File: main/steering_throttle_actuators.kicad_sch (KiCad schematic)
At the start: 2 parts, among them M2 Throttle_Motor, M3 Steering_Motor

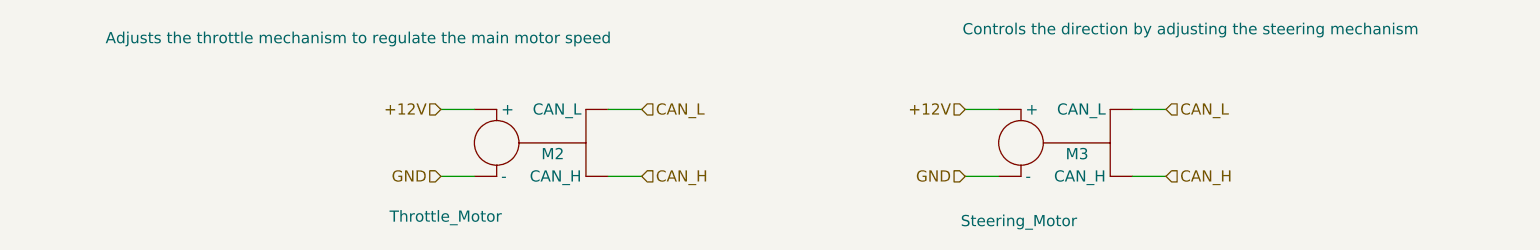
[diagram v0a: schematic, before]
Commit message: added cerbo gx and user interface sheet
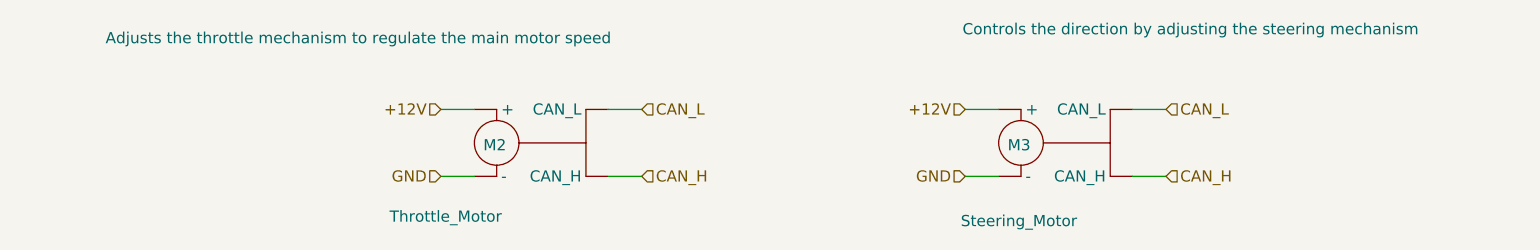
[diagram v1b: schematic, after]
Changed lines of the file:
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@@
 	)
 	(symbol
+		(lib_name "New_Library_0:Motor")
 		(lib_id "New_Library_0:Motor")
 		(at 157.48 90.17 0)
@@
 		(dnp no)
 		(property "Reference" "M3"
-			(at 162.56 91.4399 0)
+			(at 155.956 90.424 0)
 			(effects
 				(font
@@
 		(dnp no)
 		(property "Reference" "M2"
-			(at 102.87 91.4399 0)
+			(at 96.266 90.424 0)
 			(effects
 				(font

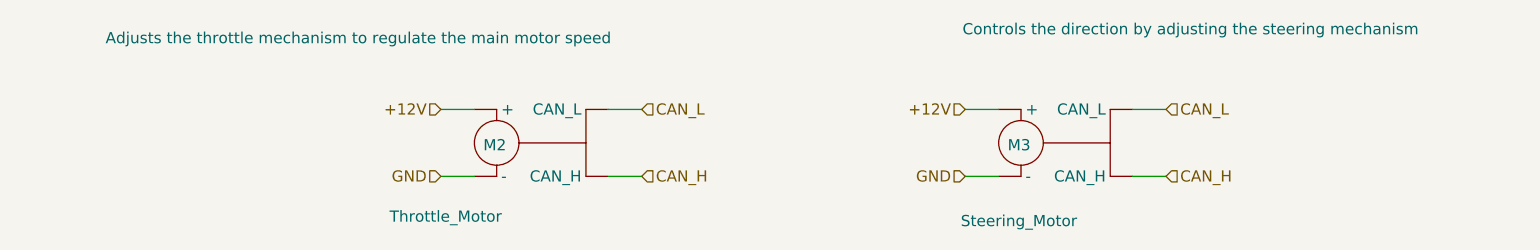
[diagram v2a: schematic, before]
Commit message: Changed name of Steering_Motor to Steering_Rod_Motor
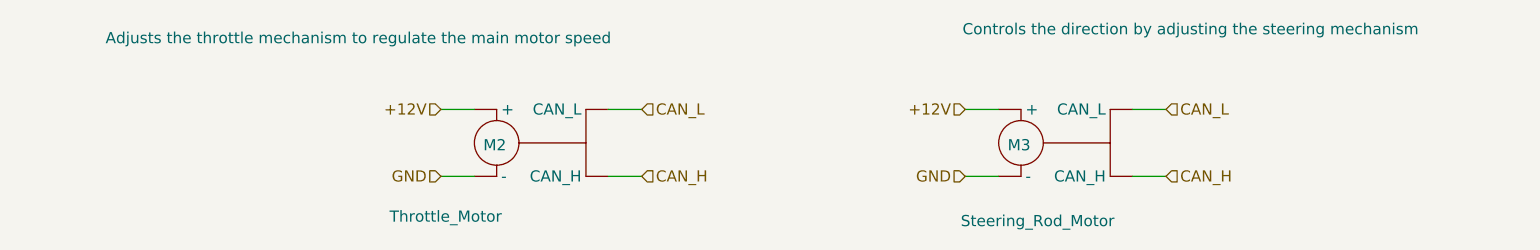
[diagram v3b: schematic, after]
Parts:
- M3: value Steering_Motor -> Steering_Rod_Motor
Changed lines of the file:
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@@
 	)
 	(symbol
+		(lib_name "New_Library_0:Motor")
 		(lib_id "New_Library_0:Motor")
 		(at 157.48 90.17 0)
@@
 			)
 		)
-		(property "Value" "Steering_Motor"
+		(property "Value" "Steering_Rod_Motor"
 			(at 150.622 99.06 0)
 			(effects

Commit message: added logos, oranised sheets, final version
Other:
- company: (none) -> Designers: Krzysztof Grajek, Wojtek Kołodziej
- title: (none) -> Steering throttle actuators schematic
